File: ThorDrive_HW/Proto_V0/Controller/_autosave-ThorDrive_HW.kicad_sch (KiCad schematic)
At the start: 56 parts, among them J1 Conn_01x04_Socket, J10 Conn_01x03_Socket, J13 CTRL, J2 Conn_01x06_Socket, J3 Conn_01x03_Socket, J4 Conn_01x08_Socket, J5 Conn_01x08_Pin, J6 Conn_01x04_Pin, J7 Conn_01x06_Pin, J8 Conn_01x04_Pin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

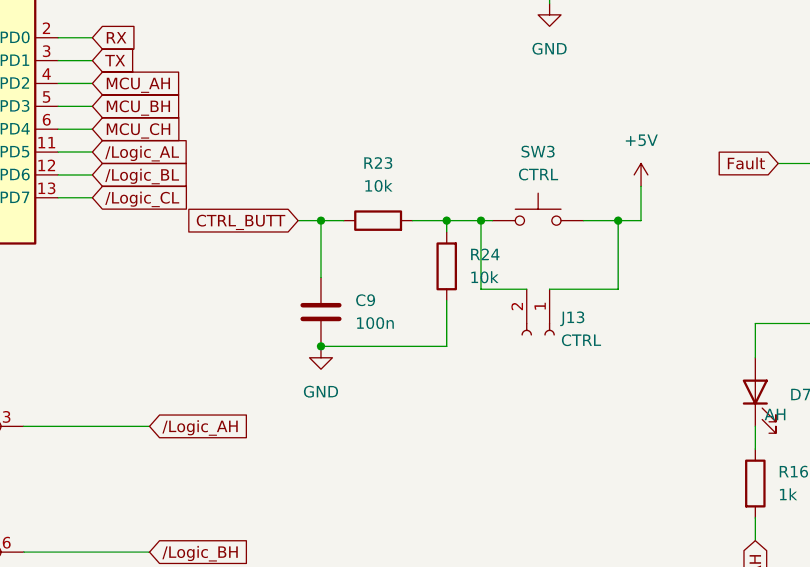
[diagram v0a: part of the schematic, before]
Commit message: Latest hardware  changes (added pulldown Resistor for CTRL button)
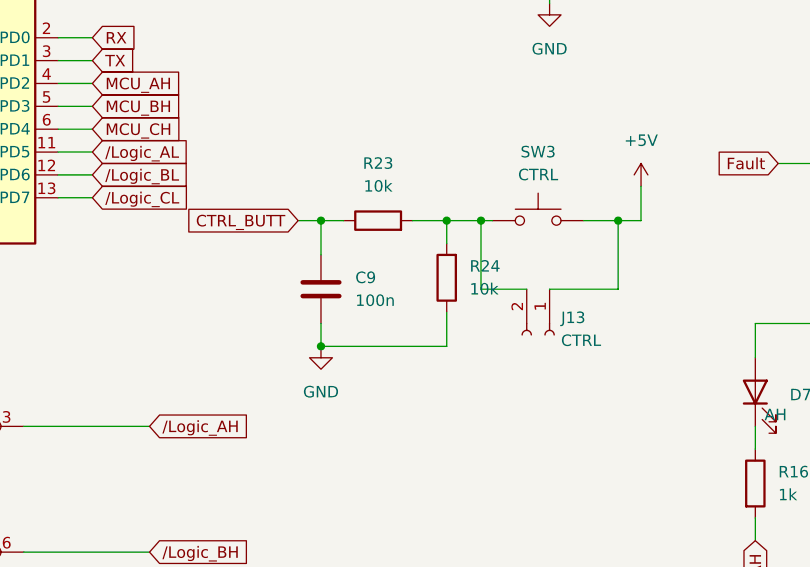
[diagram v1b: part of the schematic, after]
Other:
- moved on the sheet: C9, R24
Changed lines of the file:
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@@
 	(wire
 		(pts
-			(xy 93.98 92.71) (xy 93.98 99.06)
+			(xy 93.98 92.71) (xy 93.98 96.52)
 		)
 		(stroke
@@
 	(wire
 		(pts
-			(xy 107.95 93.98) (xy 107.95 92.71)
+			(xy 107.95 95.25) (xy 107.95 92.71)
 		)
 		(stroke
@@
 	(wire
 		(pts
+			(xy 93.98 104.14) (xy 93.98 106.68)
+		)
+		(stroke
+			(width 0)
+			(type default)
+		)
+	)
+	(wire
+		(pts
 			(xy 156.21 125.73) (xy 156.21 128.27)
 		)
@@
 	(wire
 		(pts
-			(xy 107.95 101.6) (xy 107.95 106.68)
+			(xy 107.95 102.87) (xy 107.95 106.68)
 		)
 		(stroke
@@
 	(symbol
 		(lib_id "Device:C")
-		(at 93.98 102.87 0)
+		(at 93.98 100.33 0)
 		(unit 1)
 		(exclude_from_sim no)
@@
 		(fields_autoplaced yes)
 		(property "Reference" "C9"
-			(at 97.79 101.5999 0)
+			(at 97.79 99.0599 0)
 			(effects
 				(font
@@
 		)
 		(property "Value" "100n"
-			(at 97.79 104.1399 0)
+			(at 97.79 101.5999 0)
 			(effects
 				(font
@@
 		)
 		(property "Footprint" "Capacitor_SMD:C_0805_2012Metric_Pad1.18x1.45mm_HandSolder"
-			(at 94.9452 106.68 0)
+			(at 94.9452 104.14 0)
 			(effects
 				(font
@@
 		)
 		(property "Datasheet" "~"
-			(at 93.98 102.87 0)
+			(at 93.98 100.33 0)
 			(effects
 				(font
@@
 		)
 		(property "Description" "Unpolarized capacitor"
-			(at 93.98 102.87 0)
+			(at 93.98 100.33 0)
 			(effects
 				(font
@@
 	(symbol
 		(lib_id "Device:R")
-		(at 107.95 97.79 180)
+		(at 107.95 99.06 180)
 		(unit 1)
 		(exclude_from_sim no)
@@
 		(fields_autoplaced yes)
 		(property "Reference" "R24"
-			(at 110.49 96.5199 0)
+			(at 110.49 97.7899 0)
 			(effects
 				(font
@@
 		)
 		(property "Value" "10k"
-			(at 110.49 99.0599 0)
+			(at 110.49 100.3299 0)
 			(effects
 				(font
@@
 		)
 		(property "Footprint" "Resistor_SMD:R_1206_3216Metric_Pad1.30x1.75mm_HandSolder"
-			(at 109.728 97.79 90)
+			(at 109.728 99.06 90)
 			(effects
 				(font
@@
 		)
 		(property "Datasheet" "~"
-			(at 107.95 97.79 0)
+			(at 107.95 99.06 0)
 			(effects
 				(font
@@
 		)
 		(property "Description" "Resistor"
-			(at 107.95 97.79 0)
+			(at 107.95 99.06 0)
 			(effects
 				(font
